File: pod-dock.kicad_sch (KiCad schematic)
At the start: 0 parts

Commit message: Add P1 + 500K resistor for serial
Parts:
- added P1: IPOD_CONNECTOR_MALE, symbol ipod-connector_male:IPOD_CONNECTOR_MALE
- added R1: 500K, symbol Device:R
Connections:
- new net: P1.11 (GND@11), R1.1
- new net: P1.21 (ACC_INDICATOR), R1.2
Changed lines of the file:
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@@
 	(generator_version "9.0")
 	(paper "A4")
+	(wire
+		(pts
+			(xy 127 77.47) (xy 127 85.09)
+		)
+		(stroke
+			(width 0)
+			(type default)
+		)
+	)
+	(wire
+		(pts
+			(xy 142.24 77.47) (xy 127 77.47)
+		)
+		(stroke
+			(width 0)
+			(type default)
+		)
+	)
+	(wire
+		(pts
+			(xy 127 102.87) (xy 142.24 102.87)
+		)
+		(stroke
+			(width 0)
+			(type default)
+		)
+	)
+	(wire
+		(pts
+			(xy 127 92.71) (xy 127 102.87)
+		)
+		(stroke
+			(width 0)
+			(type default)
+		)
+	)
+	(symbol
+		(lib_id "ipod-connector_male:IPOD_CONNECTOR_MALE")
+		(at 160.02 87.63 0)
+		(unit 1)
+		(exclude_from_sim no)
+		(in_bom yes)
+		(on_board yes)
+		(dnp no)
+		(fields_autoplaced yes)
+		(property "Reference" "P1"
+			(at 173.99 87.6299 0)
+			(effects
+				(font
+					(size 1.27 1.27)
+				)
+				(justify left)
+			)
+		)
+		(property "Value" "IPOD_CONNECTOR_MALE"
+			(at 173.99 90.1699 0)
+			(effects
+				(font
+					(size 1.27 1.27)
+				)
+				(justify left)
+			)
+		)
+		(property "Footprint" ""
+			(at 160.02 87.63 0)
+			(effects
+				(font
+					(size 1.524 1.524)
+				)
+			)
+		)
+		(property "Datasheet" ""
+			(at 160.02 87.63 0)
+			(effects
+				(font
+					(size 1.524 1.524)
+				)
+			)
+		)
+		(property "Description" ""
+			(at 160.02 87.63 0)
+			(effects
+				(font
+					(size 1.27 1.27)
+				)
+			)
+		)
+		(pin "24"
+		)
+		(pin "30"
+		)
+		(pin "29"
+		)
+		(pin "28"
+		)
+		(pin "27"
+		)
+		(pin "26"
+		)
+		(pin "25"
+		)
+		(pin "6"
+		)
+		(pin "5"
+		)
+		(pin "4"
+		)
+		(pin "3"
+		)
+		(pin "2"
+		)
+		(pin "1"
+		)
+		(pin "10"
+		)
+		(pin "9"
+		)
+		(pin "11"
+		)
+		(pin "12"
+		)
+		(pin "7"
+		)
+		(pin "8"
+		)
+		(pin "13"
+		)
+		(pin "14"
+		)
+		(pin "15"
+		)
+		(pin "16"
+		)
+		(pin "17"
+		)
+		(pin "18"
+		)
+		(pin "19"
+		)
+		(pin "20"
+		)
+		(pin "21"
+		)
+		(pin "22"
+		)
+		(pin "23"
+		)
+		(instances
+			(project ""
+				(path "/3473e828-3d50-4ac3-9075-478b362e3bfd"
+					(reference "P1")
+					(unit 1)
+				)
+			)
+		)
+	)
+	(symbol
+		(lib_id "Device:R")
+		(at 127 88.9 0)
+		(unit 1)
+		(exclude_from_sim no)
+		(in_bom yes)
+		(on_board yes)
+		(dnp no)
+		(fields_autoplaced yes)
+		(property "Reference" "R1"
+			(at 129.54 87.6299 0)
+			(effects
+				(font
+					(size 1.27 1.27)
+				)
+				(justify left)
+			)
+		)
+		(property "Value" "500K"
+			(at 129.54 90.1699 0)
+			(effects
+				(font
+					(size 1.27 1.27)
+				)
+				(justify left)
+			)
+		)
+		(property "Footprint" ""
+			(at 125.222 88.9 90)
+			(effects
+				(font
+					(size 1.27 1.27)
+				)
+				(hide yes)
+			)
+		)
+		(property "Datasheet" "~"
+			(at 127 88.9 0)
+			(effects
+				(font
+					(size 1.27 1.27)
+				)
+				(hide yes)
+			)
+		)
+		(property "Description" "Resistor"
+			(at 127 88.9 0)
+			(effects
+				(font
+					(size 1.27 1.27)
+				)
+				(hide yes)
+			)
+		)
+		(pin "2"
+		)
+		(pin "1"
+		)
+		(instances
+			(project ""
+				(path "/3473e828-3d50-4ac3-9075-478b362e3bfd"
+					(reference "R1")
+					(unit 1)
+				)
+			)
+		)
+	)
 	(sheet_instances
 		(path "/"

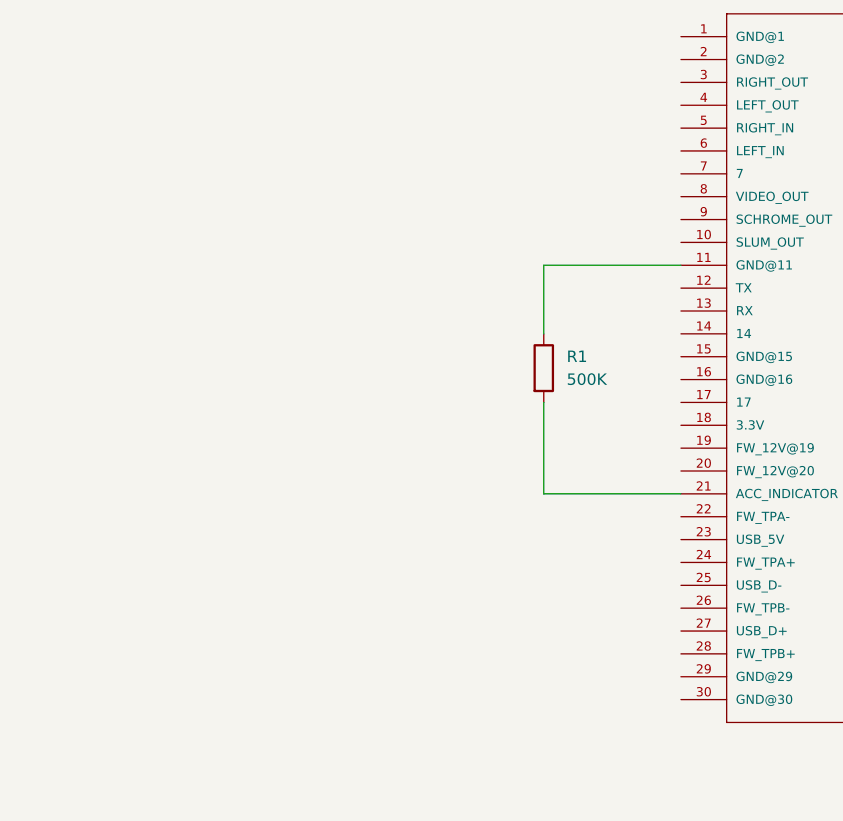
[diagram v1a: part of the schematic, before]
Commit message: Add charging connections
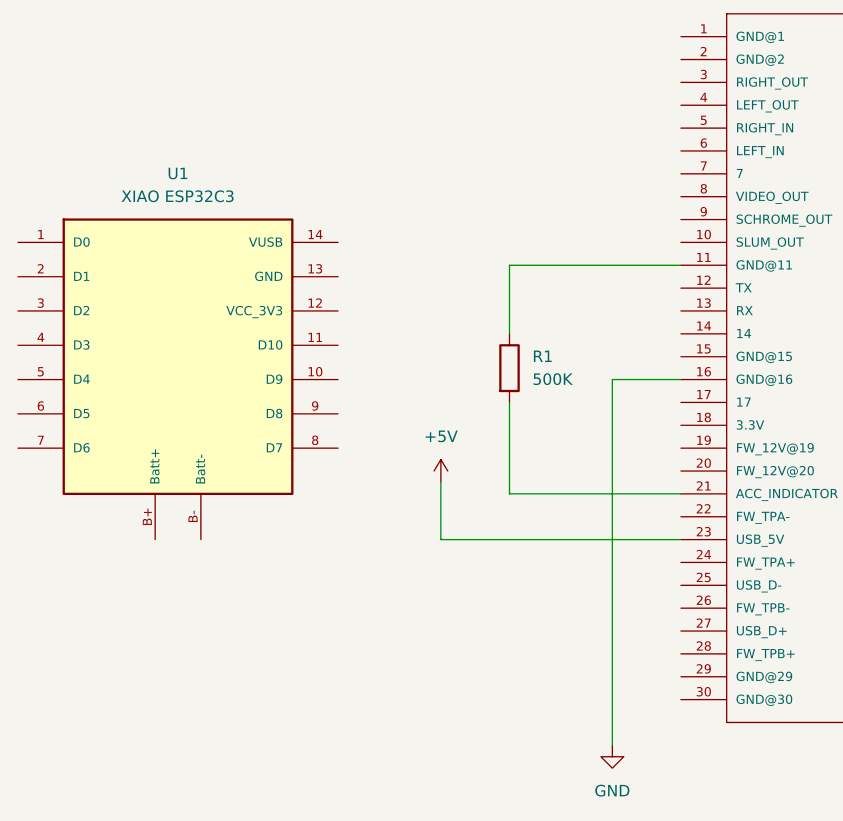
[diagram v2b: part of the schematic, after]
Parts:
- added U1: XIAO ESP32C3, XIAO_ESP32C3:xiao_esp32c3, symbol xiao_esp32c3:XIAO ESP32C3
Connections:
- net GND: now reaches P1.16 (GND@16)
- net +5V: now reaches P1.23 (USB_5V)
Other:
- moved on the sheet: R1

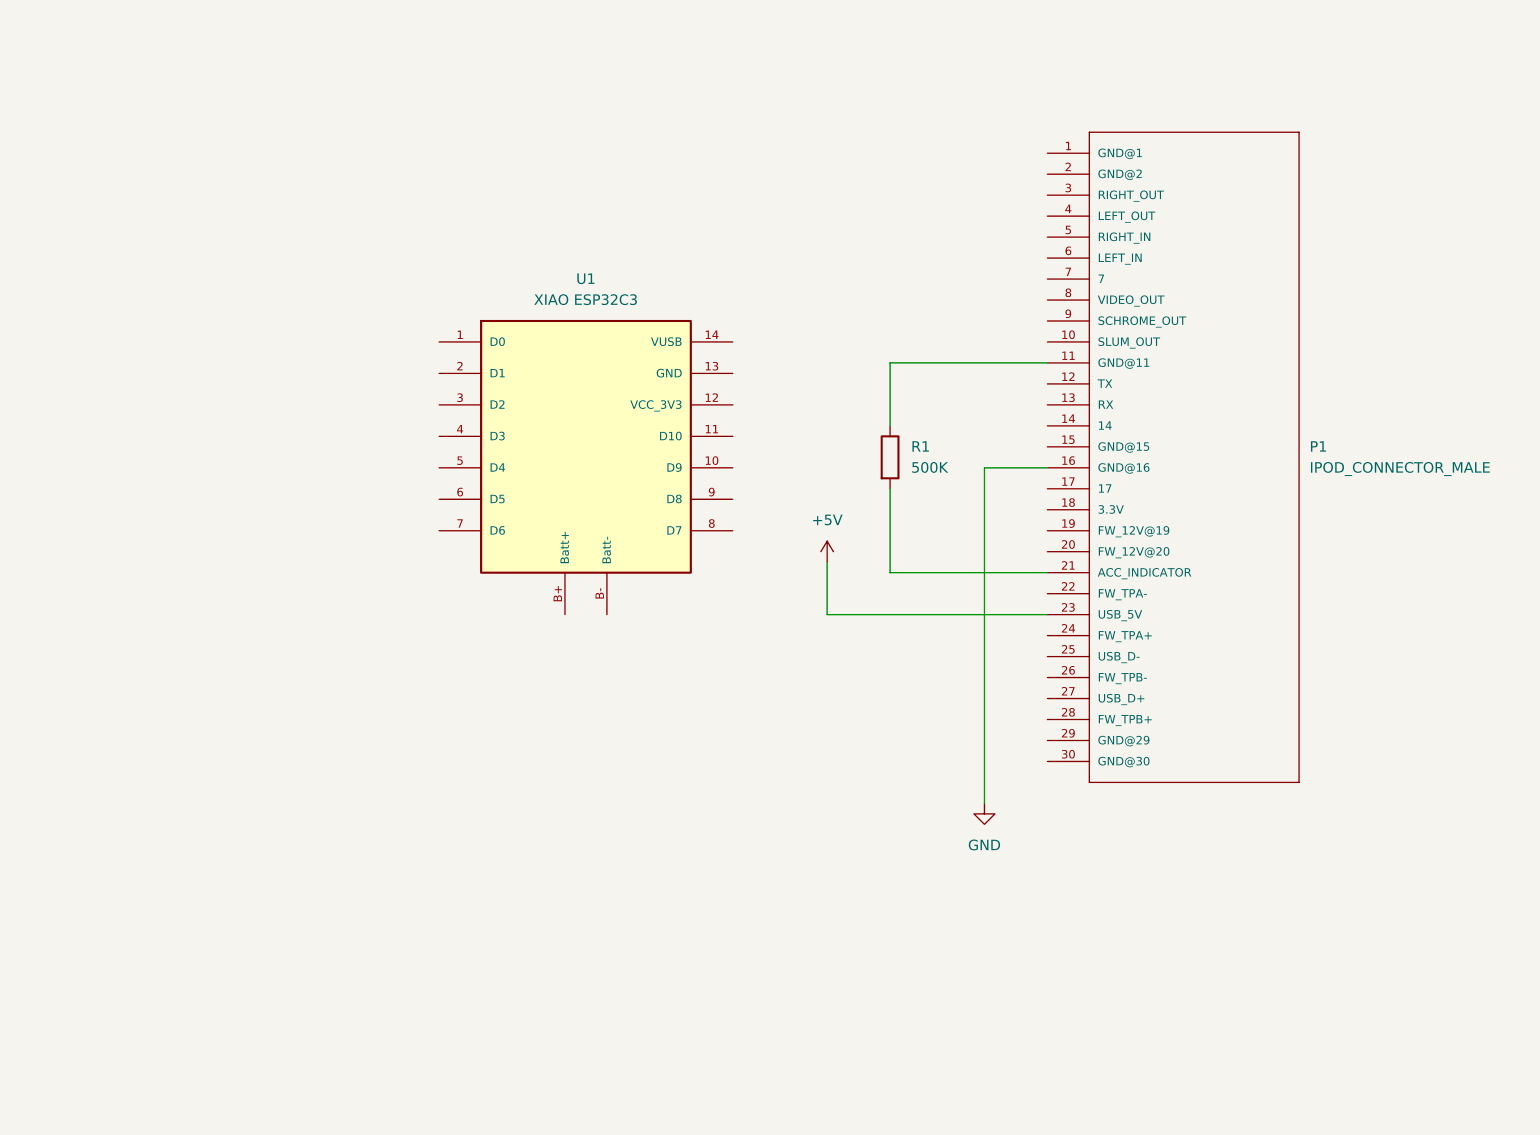
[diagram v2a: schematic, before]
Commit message: Add USB-C
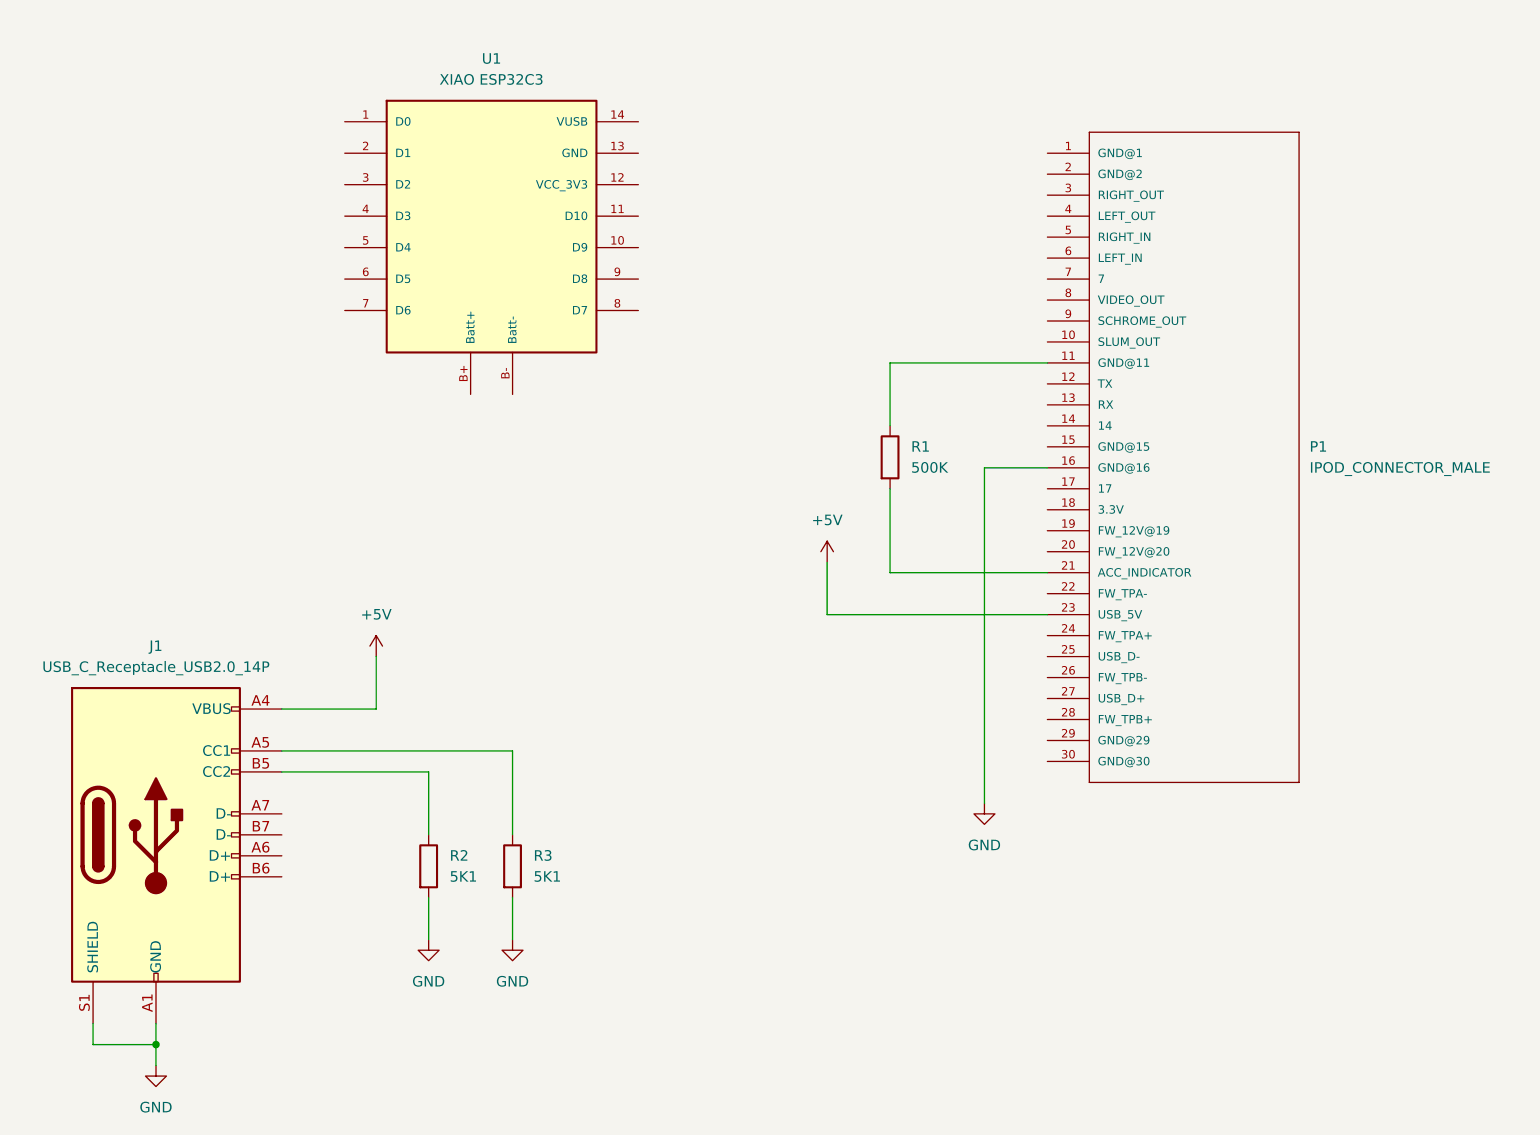
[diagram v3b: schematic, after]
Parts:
- added J1: USB_C_Receptacle_USB2.0_14P, symbol Connector:USB_C_Receptacle_USB2.0_14P
- added R2, R3: 5K1, symbol Device:R
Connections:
- net +5V: now also J1.A4 (VBUS), J1.A9 (VBUS), J1.B4 (VBUS), J1.B9 (VBUS)
- net GND: now also J1.A1 (GND), J1.A12 (GND), J1.B1 (GND), J1.B12 (GND), J1.S1 (SHIELD), R2.2, R3.2
- new net: J1.B5 (CC2), R2.1
- new net: J1.A5 (CC1), R3.1
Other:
- moved on the sheet: U1

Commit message: Update pod-dock.kicad_sch
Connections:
- net GND: now also P1.1 (GND@1), P1.11 (GND@11), P1.15 (GND@15), P1.2 (GND@2), P1.29 (GND@29), P1.30 (GND@30), R1.1
- net D-: now reaches P1.25 (USB_D-)
- net D-: now also J1.A7 (D-), J1.B7 (D-)
- net D+: now reaches P1.27 (USB_D+)
- net D+: now also J1.A6 (D+), J1.B6 (D+)

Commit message: Update pod-dock.kicad_sch
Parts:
- added J2: AUDIO OUT, symbol Connector:Conn_01x03_Pin
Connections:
- net GND: no longer P1.1 (GND@1), P1.11 (GND@11), P1.15 (GND@15), P1.16 (GND@16), P1.2 (GND@2), P1.29 (GND@29), P1.30 (GND@30), R1.1
- net RX: now reaches P1.12 (TX)
- net TX: now reaches P1.13 (RX)
- net +12V: now reaches P1.19 (FW_12V@19)
- net +12V: now also P1.20 (FW_12V@20)
- net GNDS: now reaches P1.21 (ACC_INDICATOR), R1.2
- net at P1.3 (RIGHT_OUT): now also J2.2 (Pin_2)
- net at P1.4 (LEFT_OUT): now also J2.3 (Pin_3)
- new net: J2.1 (Pin_1), P1.1 (GND@1), P1.2 (GND@2)
- new net: P1.11 (GND@11), R1.1
- new net GNDPWR: P1.15 (GND@15), P1.16 (GND@16), P1.29 (GND@29), P1.30 (GND@30)
- no-connect marks 0 -> 13
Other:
- moved on the sheet: R2, R3

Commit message: Update pod-dock.kicad_sch
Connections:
- net GNDPWR is gone; now on net GND: P1.15 (GND@15), P1.16 (GND@16), P1.29 (GND@29), P1.30 (GND@30)
- net GNDS is gone; now on net GND: P1.21 (ACC_INDICATOR), R1.2
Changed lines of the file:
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@@
-	)
-	(symbol
-		(lib_id "power:GNDPWR")
-		(at 134.62 130.81 0)
-		(unit 1)
-		(exclude_from_sim no)
-		(in_bom yes)
-		(on_board yes)
-		(dnp no)
-		(fields_autoplaced yes)
-		(property "Reference" "#PWR01"
-			(at 134.62 135.89 0)
-			(effects
-				(font
-					(size 1.27 1.27)
-				)
-				(hide yes)
-			)
-		)
-		(property "Value" "GNDPWR"
-			(at 134.493 134.62 0)
-			(effects
-				(font
-					(size 1.27 1.27)
-				)
-			)
-		)
-		(property "Footprint" ""
-			(at 134.62 132.08 0)
-			(effects
-				(font
-					(size 1.27 1.27)
-				)
-				(hide yes)
-			)
-		)
-		(property "Datasheet" ""
-			(at 134.62 132.08 0)
-			(effects
-				(font
-					(size 1.27 1.27)
-				)
-				(hide yes)
-			)
-		)
-		(property "Description" "Power symbol creates a global label with name \"GNDPWR\" , global ground"
-			(at 134.62 130.81 0)
-			(effects
-				(font
-					(size 1.27 1.27)
-				)
-				(hide yes)
-			)
-		)
-		(pin "1"
-		)
-		(instances
-			(project ""
-				(path "/3473e828-3d50-4ac3-9075-478b362e3bfd"
-					(reference "#PWR01")
-					(unit 1)
-				)
-			)
-		)
 	)
 	(symbol
@@
 	)
 	(symbol
+		(lib_id "power:GND")
+		(at 134.62 130.81 0)
+		(unit 1)
+		(exclude_from_sim no)
+		(in_bom yes)
+		(on_board yes)
+		(dnp no)
+		(fields_autoplaced yes)
+		(property "Reference" "#PWR07"
+			(at 134.62 137.16 0)
+			(effects
+				(font
+					(size 1.27 1.27)
+				)
+				(hide yes)
+			)
+		)
+		(property "Value" "GND"
+			(at 134.62 135.89 0)
+			(effects
+				(font
+					(size 1.27 1.27)
+				)
+			)
+		)
+		(property "Footprint" ""
+			(at 134.62 130.81 0)
+			(effects
+				(font
+					(size 1.27 1.27)
+				)
+				(hide yes)
+			)
+		)
+		(property "Datasheet" ""
+			(at 134.62 130.81 0)
+			(effects
+				(font
+					(size 1.27 1.27)
+				)
+				(hide yes)
+			)
+		)
+		(property "Description" "Power symbol creates a global label with name \"GND\" , ground"
+			(at 134.62 130.81 0)
+			(effects
+				(font
+					(size 1.27 1.27)
+				)
+				(hide yes)
+			)
+		)
+		(pin "1"
+		)
+		(instances
+			(project ""
+				(path "/3473e828-3d50-4ac3-9075-478b362e3bfd"
+					(reference "#PWR07")
+					(unit 1)
+				)
+			)
+		)
+	)
+	(symbol
 		(lib_id "Device:R")
 		(at 60.96 138.43 0)
@@
 	)
 	(symbol
-		(lib_id "power:GNDS")
+		(lib_id "power:GND")
 		(at 123.19 111.76 0)
 		(unit 1)
@@
 		(dnp no)
 		(fields_autoplaced yes)
-		(property "Reference" "#PWR07"
+		(property "Reference" "#PWR01"
 			(at 123.19 118.11 0)
 			(effects
@@
 			)
 		)
-		(property "Value" "GNDS"
+		(property "Value" "GND"
 			(at 123.19 116.84 0)
 			(effects
@@
 			)
 		)
-		(property "Description" "Power symbol creates a global label with name \"GNDS\" , signal ground"
+		(property "Description" "Power symbol creates a global label with name \"GND\" , ground"
 			(at 123.19 111.76 0)
 			(effects
@@
 			(project ""
 				(path "/3473e828-3d50-4ac3-9075-478b362e3bfd"
-					(reference "#PWR07")
-					(unit 1)
-				)
+					(reference "#PWR01")
+					(unit 1)
+				)

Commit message: Update pod-dock.kicad_sch
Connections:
- net +5V: now also U1.14 (VUSB)
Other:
- moved on the sheet: J1, R2, R3
